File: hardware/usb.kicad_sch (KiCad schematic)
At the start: 7 parts

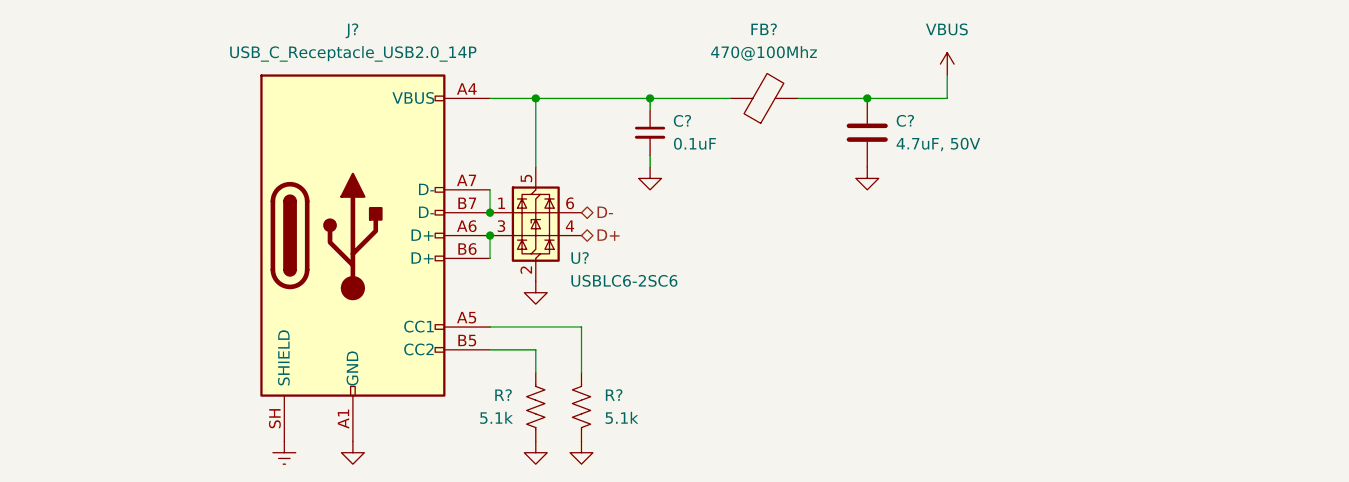
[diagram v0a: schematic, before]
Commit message: Update LEDs
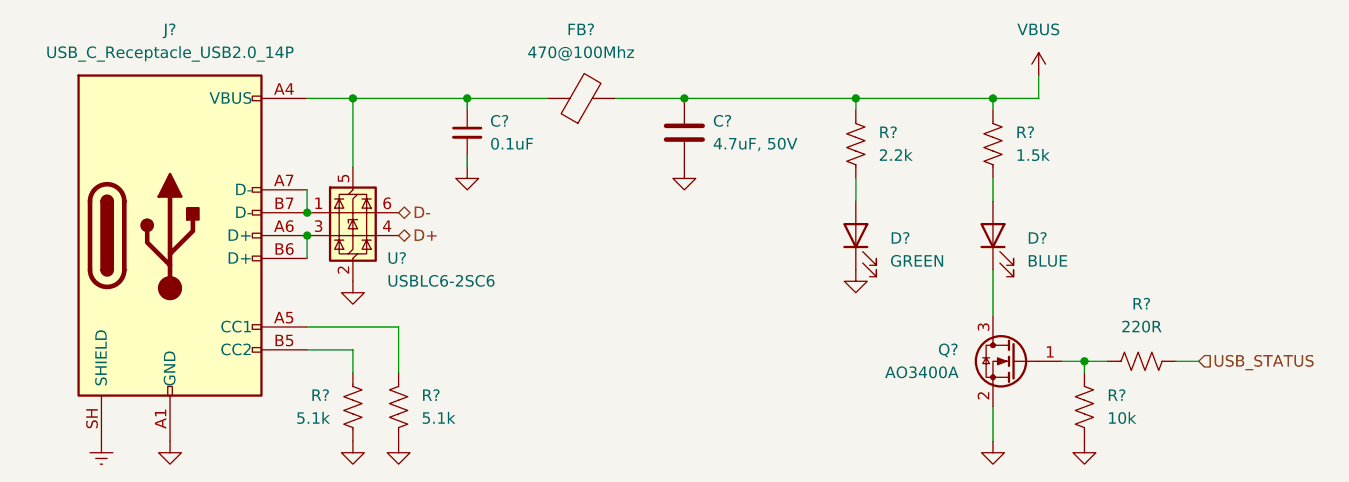
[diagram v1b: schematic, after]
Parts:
- added D?: BLUE, Diode_SMD:D_0805_2012Metric, symbol Device:LED
- added D?: GREEN, Diode_SMD:D_0805_2012Metric, symbol Device:LED
- added Q?: AO3400A, Package_TO_SOT_SMD:SOT-23, symbol Transistor_FET:AO3400A
- added R?: 1.5k, Resistor_SMD:R_0603_1608Metric, symbol Device:R_US
- added R?: 220R, Resistor_SMD:R_0603_1608Metric, symbol Device:R_US
- added R?: 10k, Resistor_SMD:R_0603_1608Metric, symbol Device:R_US
- added R?: 2.2k, Resistor_SMD:R_0603_1608Metric, symbol Device:R_US
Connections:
- net GND: now also D?.1 (K), Q?.2 (S), R?.2
- net VBUS: now also R?.1, R?.1
- new net: D?.2 (A), R?.2 (x2)
- new net: Q?.1 (G), R?.1, R?.1
- new net: D?.1 (K), Q?.3 (D)
- new net USB_STATUS: R?.2
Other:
- moved on the sheet: C?, FB?, J?, R?, U?

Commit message: TMC2209 Schematic Improvements
Sense resistors and status LEDs
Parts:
- removed R?: 220R, Resistor_SMD:R_0603_1608Metric, symbol Device:R_US
- added R?: 100R, Resistor_SMD:R_0603_1608Metric, symbol Device:R_US
- C?: value 4.7uF, 50V -> 4.7uF, 16V; footprint Capacitor_SMD:C_1206_3216Metric_Pad1.33x1.80mm_HandSolder -> Capacitor_SMD:C_0805_2012Metric; Part Number CL31B475KBHNFNE -> GCM21BR71C475KA73L; Vendor URL https://www.digikey.com/en/products/detail/samsung-electro-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 -> https://www.digikey.com/en/products/detail/murata-electroni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
- Q?: Part Number (none) -> AO3400A; Vendor URL (none) -> https://www.digikey.com/en/products/detail/alpha-omega-semi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
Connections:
- net USB_STATUS: now also R?.2
- net at Q?.1 (G), R?.1: now also R?.1
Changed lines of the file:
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@@
+			)
+		)
+		(property "Part Number" "AO3400A"
+			(at 186.69 116.84 0)
+			(hide yes)
+			(show_name no)
+			(do_not_autoplace no)
+			(effects
+				(font
+					(size 1.27 1.27)
+				)
+			)
+		)
+		(property "Vendor URL" "https://www.digikey.com/en/products/detail/alpha-omega-semiconductor-inc/AO3400A/1855772"
+			(at 186.69 116.84 0)
+			(hide yes)
+			(show_name no)
+			(do_not_autoplace no)
+			(effects
+				(font
+					(size 1.27 1.27)
+				)
 			)
 		)
@@
 	)
 	(symbol
+		(lib_id "Device:R_US")
+		(at 200.66 116.84 90)
+		(mirror x)
+		(unit 1)
+		(body_style 1)
+		(exclude_from_sim no)
+		(in_bom yes)
+		(on_board yes)
+		(in_pos_files yes)
+		(dnp no)
+		(property "Reference" "R?"
+			(at 200.66 111.76 90)
+			(show_name no)
+			(do_not_autoplace no)
+			(effects
+				(font
+					(size 1.27 1.27)
+				)
+			)
+		)
+		(property "Value" "100R"
+			(at 200.66 114.3 90)
+			(show_name no)
+			(do_not_autoplace no)
+			(effects
+				(font
+					(size 1.27 1.27)
+				)
+			)
+		)
+		(property "Footprint" "Resistor_SMD:R_0603_1608Metric"
+			(at 200.914 117.856 90)
+			(hide yes)
+			(show_name no)
+			(do_not_autoplace no)
+			(effects
+				(font
+					(size 1.27 1.27)
+				)
+			)
+		)
+		(property "Datasheet" ""
+			(at 200.66 116.84 0)
+			(hide yes)
+			(show_name no)
+			(do_not_autoplace no)
+			(effects
+				(font
+					(size 1.27 1.27)
+				)
+			)
+		)
+		(property "Description" "Resistor, US symbol"
+			(at 200.66 116.84 0)
+			(hide yes)
+			(show_name no)
+			(do_not_autoplace no)
+			(effects
+				(font
+					(size 1.27 1.27)
+				)
+			)
+		)
+		(property "Part Number" "RC0603FR-07100RL"
+			(at 200.66 116.84 0)
+			(hide yes)
+			(show_name no)
+			(do_not_autoplace no)
+			(effects
+				(font
+					(size 1.27 1.27)
+				)
+			)
+		)
+		(property "Vendor URL" "https://www.digikey.com/en/products/detail/yageo/RC0603FR-07100RL/726888"
+			(at 200.66 116.84 0)
+			(hide yes)
+			(show_name no)
+			(do_not_autoplace no)
+			(effects
+				(font
+					(size 1.27 1.27)
+				)
+			)
+		)
+		(pin "1"
+		)
+		(pin "2"
+		)
+		(instances
+			(project "stepping-stone"
+				(path "/793a882e-3f7b-468b-a863-41a1f527e1bf/57b4c7a6-0892-4cab-a0ed-f935f784d7ce"
+					(reference "R?")
+					(unit 1)
+				)
+			)
+		)
+	)
+	(symbol
 		(lib_id "power:GND")
 		(at 113.03 125.73 0)
@@
 				(path "/793a882e-3f7b-468b-a863-41a1f527e1bf/57b4c7a6-0892-4cab-a0ed-f935f784d7ce"
 					(reference "#PWR014")
-					(unit 1)
-				)
-			)
-		)
-	)
-	(symbol
-		(lib_id "Device:R_US")
-		(at 200.66 116.84 90)
-		(unit 1)
-		(body_style 1)
-		(exclude_from_sim no)
-		(in_bom yes)
-		(on_board yes)
-		(in_pos_files yes)
-		(dnp no)
-		(fields_autoplaced yes)
-		(property "Reference" "R?"
-			(at 200.66 110.49 90)
-			(show_name no)
-			(do_not_autoplace no)
-			(effects
-				(font
-					(size 1.27 1.27)
-				)
-			)
-		)
-		(property "Value" "220R"
-			(at 200.66 113.03 90)
-			(show_name no)
-			(do_not_autoplace no)
-			(effects
-				(font
-					(size 1.27 1.27)
-				)
-			)
-		)
-		(property "Footprint" "Resistor_SMD:R_0603_1608Metric"
-			(at 200.914 115.824 90)
-			(hide yes)
-			(show_name no)
-			(do_not_autoplace no)
-			(effects
-				(font
-					(size 1.27 1.27)
-				)
-			)
-		)
-		(property "Datasheet" ""
-			(at 200.66 116.84 0)
-			(hide yes)
-			(show_name no)
-			(do_not_autoplace no)
-			(effects
-				(font
-					(size 1.27 1.27)
-				)
-			)
-		)
-		(property "Description" "Resistor, US symbol"
-			(at 200.66 116.84 0)
-			(hide yes)
-			(show_name no)
-			(do_not_autoplace no)
-			(effects
-				(font
-					(size 1.27 1.27)
-				)
-			)
-		)
-		(property "Part Number" "RMCF0603JT220R"
-			(at 200.66 116.84 0)
-			(hide yes)
-			(show_name no)
-			(do_not_autoplace no)
-			(effects
-				(font
-					(size 1.27 1.27)
-				)
-			)
-		)
-		(property "Vendor URL" "https://www.digikey.com/en/products/detail/stackpole-electronics-inc/RMCF0603JT220R/1758014"
-			(at 200.66 116.84 0)
-			(hide yes)
-			(show_name no)
-			(do_not_autoplace no)
-			(effects
-				(font
-					(size 1.27 1.27)
-				)
-			)
-		)
-		(pin "1"
-		)
-		(pin "2"
-		)
-		(instances
-			(project "stepping-stone"
-				(path "/793a882e-3f7b-468b-a863-41a1f527e1bf/57b4c7a6-0892-4cab-a0ed-f935f784d7ce"
-					(reference "R?")
 					(unit 1)
 				)
@@
 			)
 		)
-		(property "Value" "4.7uF, 50V"
+		(property "Value" "4.7uF, 16V"
 			(at 153.035 92.7099 0)
 			(show_name no)
@@
 			)
 		)
-		(property "Footprint" "Capacitor_SMD:C_1206_3216Metric_Pad1.33x1.80mm_HandSolder"
+		(property "Footprint" "Capacitor_SMD:C_0805_2012Metric"
 			(at 150.8252 95.25 0)
 			(hide yes)
@@
 			)
 		)
-		(property "Part Number" "CL31B475KBHNFNE"
+		(property "Part Number" "GCM21BR71C475KA73L"
 			(at 149.86 91.44 0)
 			(hide yes)
@@
 			)
 		)
-		(property "Vendor URL" "https://www.digikey.com/en/products/detail/samsung-electro-mechanics/CL31B475KBHNFNE/3888837"
+		(property "Vendor URL" "https://www.digikey.com/en/products/detail/murata-electronics/GCM21BR71C475KA73L/2075311"
 			(at 149.86 91.44 0)
 			(hide yes)

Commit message: SD Card Pull Ups and ESD
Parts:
- U?: Part Number (none) -> USBLC6-2SC6; Vendor URL (none) -> https://www.digikey.com/en/products/detail/stmicroelectroni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
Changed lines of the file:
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@@
+			)
+		)
+		(property "Part Number" "USBLC6-2SC6"
+			(at 113.03 100.33 0)
+			(hide yes)
+			(show_name no)
+			(do_not_autoplace no)
+			(effects
+				(font
+					(size 1.27 1.27)
+				)
+			)
+		)
+		(property "Vendor URL" "https://www.digikey.com/en/products/detail/stmicroelectronics/USBLC6-2SC6/1040559"
+			(at 113.03 100.33 0)
+			(hide yes)
+			(show_name no)
+			(do_not_autoplace no)
+			(effects
+				(font
+					(size 1.27 1.27)
+				)
 			)
 		)

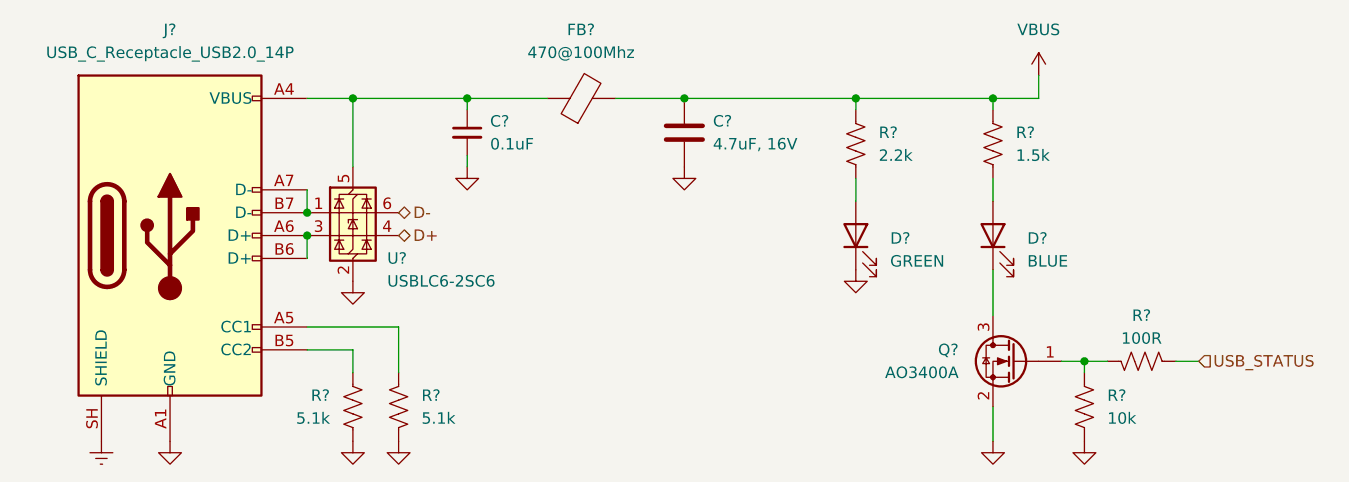
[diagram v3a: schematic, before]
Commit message: Change blue LEDs
Remove extra 5V blue LED driving for simple 3.3V driving instead
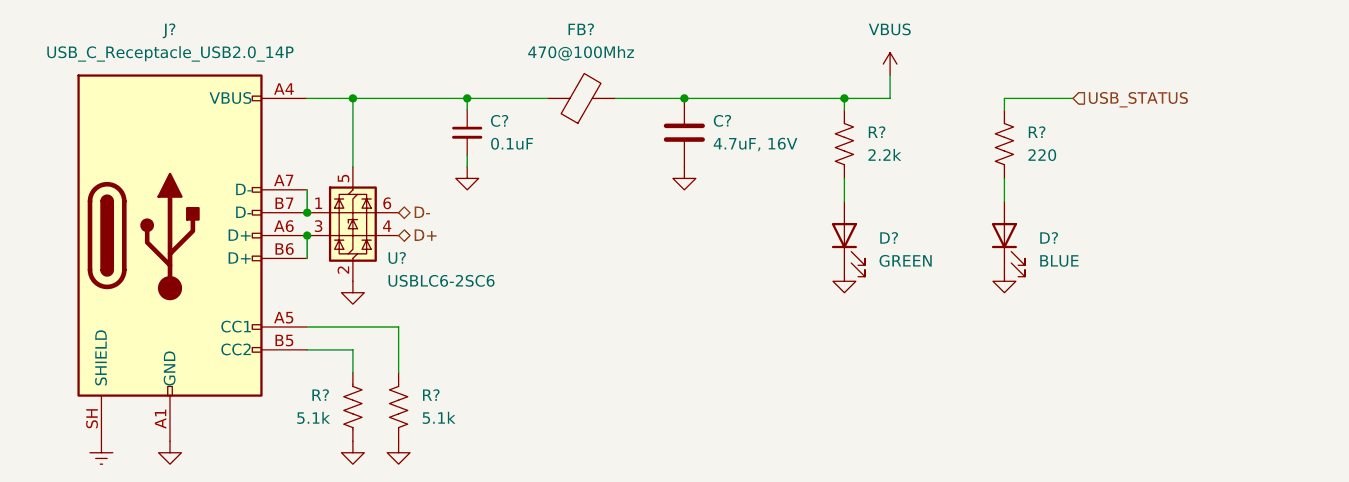
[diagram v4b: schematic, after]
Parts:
- removed D?: BLUE, Diode_SMD:D_0805_2012Metric, symbol Device:LED
- removed Q?: AO3400A, Package_TO_SOT_SMD:SOT-23, symbol Transistor_FET:AO3400A
- removed R?: 1.5k, Resistor_SMD:R_0603_1608Metric, symbol Device:R_US
- removed R?: 100R, Resistor_SMD:R_0603_1608Metric, symbol Device:R_US
- removed R?: 10k, Resistor_SMD:R_0603_1608Metric, symbol Device:R_US
- added D?: BLUE, Diode_SMD:D_0805_2012Metric, symbol Device:LED
- added R?: 220, Resistor_SMD:R_0603_1608Metric, symbol Device:R_US
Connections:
- net GND: now also D?.1 (K)
- net USB_STATUS: now also R?.1
- new net: D?.2 (A), R?.2
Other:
- moved on the sheet: D?, R?

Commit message: Add QSPI Flash
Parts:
- gave numbers to parts that had none: 11
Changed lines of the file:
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@@
 		(in_pos_files yes)
 		(dnp no)
-		(property "Reference" "R?"
+		(property "Reference" "R15"
 			(at 187.96 91.4399 0)
 			(show_name no)
@@
 			(project "stepping-stone"
 				(path "/793a882e-3f7b-468b-a863-41a1f527e1bf/57b4c7a6-0892-4cab-a0ed-f935f784d7ce"
-					(reference "R?")
+					(reference "R15")
 					(unit 1)
 				)
@@
 		(in_pos_files yes)
 		(dnp no)
-		(property "Reference" "R?"
+		(property "Reference" "R16"
 			(at 110.49 120.6499 0)
 			(show_name no)
@@
 			(project "stepping-stone"
 				(path "/793a882e-3f7b-468b-a863-41a1f527e1bf/57b4c7a6-0892-4cab-a0ed-f935f784d7ce"
-					(reference "R?")
+					(reference "R16")
 					(unit 1)
 				)
@@
 		(in_pos_files yes)
 		(dnp no)
-		(property "Reference" "C?"
+		(property "Reference" "C10"
 			(at 128.27 90.1762 0)
 			(show_name no)
@@
 			(project "stepping-stone"
 				(path "/793a882e-3f7b-468b-a863-41a1f527e1bf/57b4c7a6-0892-4cab-a0ed-f935f784d7ce"
-					(reference "C?")
+					(reference "C10")
 					(unit 1)
 				)
@@
 		(dnp no)
 		(fields_autoplaced yes)
-		(property "Reference" "J?"
+		(property "Reference" "J3"
 			(at 92.71 80.01 0)
 			(show_name no)
@@
 			(project "stepping-stone"
 				(path "/793a882e-3f7b-468b-a863-41a1f527e1bf/57b4c7a6-0892-4cab-a0ed-f935f784d7ce"
-					(reference "J?")
+					(reference "J3")
 					(unit 1)
 				)
@@
 		(in_pos_files yes)
 		(dnp no)
-		(property "Reference" "C?"
+		(property "Reference" "C11"
 			(at 153.035 90.1699 0)
 			(show_name no)
@@
 			(project "stepping-stone"
 				(path "/793a882e-3f7b-468b-a863-41a1f527e1bf/57b4c7a6-0892-4cab-a0ed-f935f784d7ce"
-					(reference "C?")
+					(reference "C11")
 					(unit 1)
 				)
@@
 		(in_pos_files yes)
 		(dnp no)
-		(property "Reference" "R?"
+		(property "Reference" "R17"
 			(at 120.65 120.6499 0)
 			(show_name no)
@@
 			(project "stepping-stone"
 				(path "/793a882e-3f7b-468b-a863-41a1f527e1bf/57b4c7a6-0892-4cab-a0ed-f935f784d7ce"
-					(reference "R?")
+					(reference "R17")
 					(unit 1)
 				)
@@
 		(in_pos_files yes)
 		(dnp no)
-		(property "Reference" "D?"
+		(property "Reference" "D9"
 			(at 189.23 103.1874 90)
 			(show_name no)
@@
 			(project "stepping-stone"
 				(path "/793a882e-3f7b-468b-a863-41a1f527e1bf/57b4c7a6-0892-4cab-a0ed-f935f784d7ce"
-					(reference "D?")
+					(reference "D9")
 					(unit 1)
 				)
@@
 		(in_pos_files yes)
 		(dnp no)
-		(property "Reference" "U?"
+		(property "Reference" "U3"
 			(at 116.84 105.41 0)
 			(show_name no)
@@
 			(project "stepping-stone"
 				(path "/793a882e-3f7b-468b-a863-41a1f527e1bf/57b4c7a6-0892-4cab-a0ed-f935f784d7ce"
-					(reference "U?")
+					(reference "U3")
 					(unit 1)
 				)
@@
 		(dnp no)
 		(fields_autoplaced yes)
-		(property "Reference" "D?"
+		(property "Reference" "D8"
 			(at 171.45 103.1874 90)
 			(show_name no)
@@
 			(project "stepping-stone"
 				(path "/793a882e-3f7b-468b-a863-41a1f527e1bf/57b4c7a6-0892-4cab-a0ed-f935f784d7ce"
-					(reference "D?")
+					(reference "D8")
 					(unit 1)
 				)
@@
 		(dnp no)
 		(fields_autoplaced yes)
-		(property "Reference" "FB?"
+		(property "Reference" "FB1"
 			(at 138.3792 80.01 90)
 			(show_name no)
@@
 			(project "stepping-stone"
 				(path "/793a882e-3f7b-468b-a863-41a1f527e1bf/57b4c7a6-0892-4cab-a0ed-f935f784d7ce"
-					(reference "FB?")
+					(reference "FB1")
 					(unit 1)
 				)
@@
 		(dnp no)
 		(fields_autoplaced yes)
-		(property "Reference" "R?"
+		(property "Reference" "R14"
 			(at 170.18 91.4399 0)
 			(show_name no)
@@
 			(project "stepping-stone"
 				(path "/793a882e-3f7b-468b-a863-41a1f527e1bf/57b4c7a6-0892-4cab-a0ed-f935f784d7ce"
-					(reference "R?")
+					(reference "R14")
 					(unit 1)
 				)
